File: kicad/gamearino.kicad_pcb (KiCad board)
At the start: 2 copper layers, 13 parts, among them Q1 FDN338P, Q2 FDN335N, Q3 PMBT3904, Q4 PMBT3906, SW1 Left, SW2 Up, SW3 Down, SW4 Right, SW5 Select, SW6 Start, SW7 B, SW8 A, U1 ESP-12F

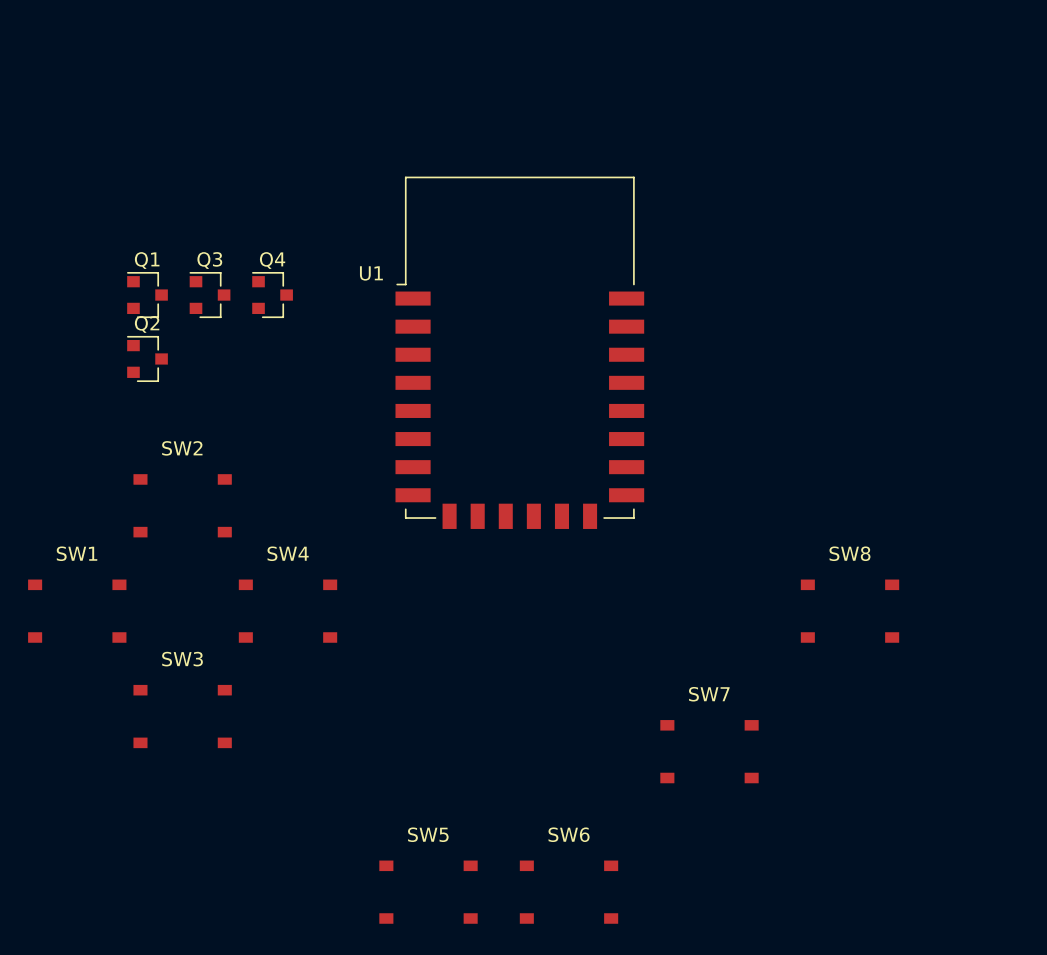
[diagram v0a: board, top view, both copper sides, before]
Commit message: PCB-Platzierung, 3D-Knöpfe, Schaltung wird noch getestet
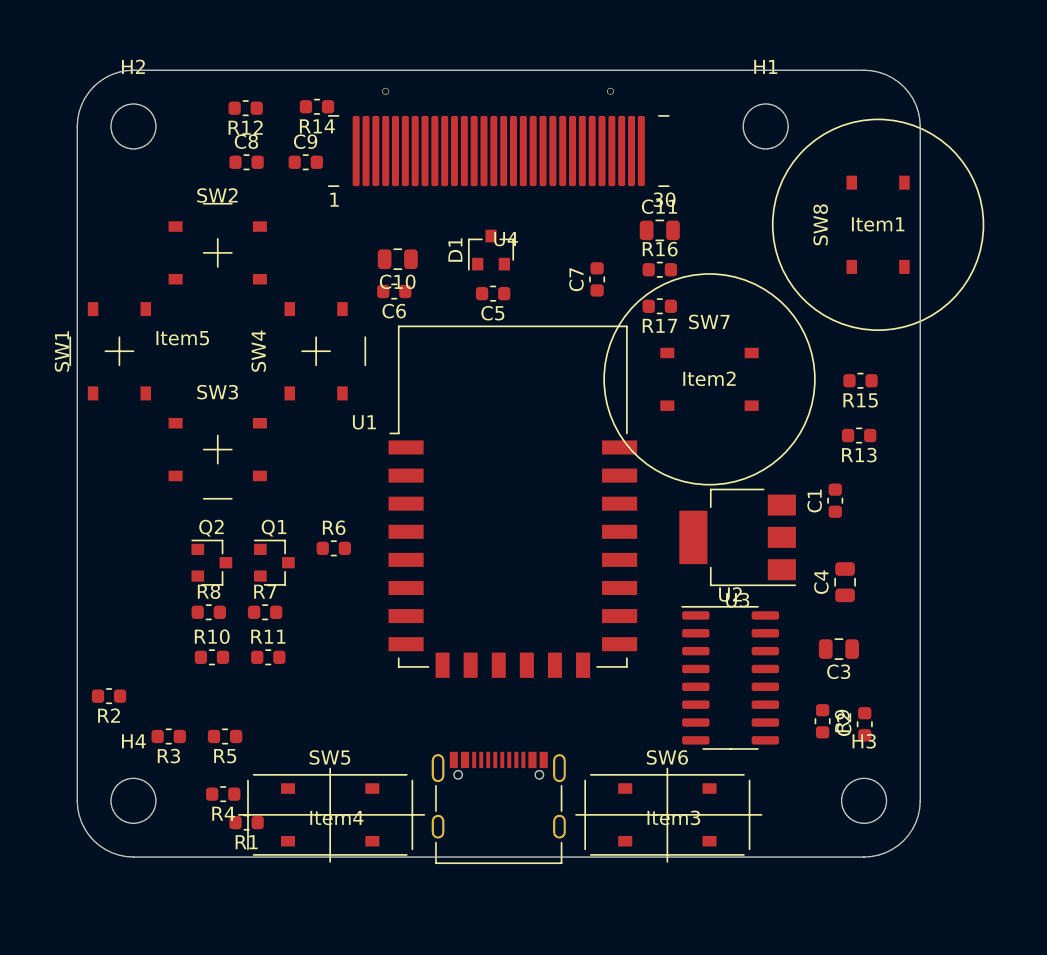
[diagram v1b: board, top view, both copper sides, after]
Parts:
- removed Q3: PMBT3904, Package_TO_SOT_SMD:SOT-23
- removed Q4: PMBT3906, Package_TO_SOT_SMD:SOT-23
- added C1: 100n, Capacitor_SMD:C_0603_1608Metric, F.Cu at (153.9, 74.6)
- added C10: 4u7, Capacitor_SMD:C_0805_2012Metric, F.Cu at (122.8, 57.5)
- added C11: 2u2, Capacitor_SMD:C_0805_2012Metric, F.Cu at (141.5, 55.4)
- added C2: 100n, Capacitor_SMD:C_0603_1608Metric, F.Cu at (156.1, 90.5)
- added C3: 10u/16V/X5R, Capacitor_SMD:C_0805_2012Metric, F.Cu at (154.2, 85.2)
- added C4: 10u/16V/X5R, Capacitor_SMD:C_0805_2012Metric, F.Cu at (154.7, 80.4)
- added C5: 1u, Capacitor_SMD:C_0603_1608Metric, F.Cu at (129.6, 59.9)
- added C6: 1u, Capacitor_SMD:C_0603_1608Metric, F.Cu at (122.6, 59.8)
- added C7: 1u, Capacitor_SMD:C_0603_1608Metric, F.Cu at (137.0, 58.9)
- added C8: 1u, Capacitor_SMD:C_0603_1608Metric, F.Cu at (112.0, 50.5)
- added C9: 1u, Capacitor_SMD:C_0603_1608Metric, F.Cu at (116.3, 50.5)
- added D1: 1N4148, Package_TO_SOT_SMD:SOT-23, F.Cu at (129.4, 56.8)
- added H1: MountingHole, MountingHole:MountingHole_3.2mm_M3, F.Cu at (149.0, 48.0)
- added H2: MountingHole, MountingHole:MountingHole_3.2mm_M3, F.Cu at (104.0, 48.0)
- added H3: MountingHole, MountingHole:MountingHole_3.2mm_M3, F.Cu at (156.0, 96.0)
- added H4: MountingHole, MountingHole:MountingHole_3.2mm_M3, F.Cu at (104.0, 96.0)
- added Item1: 3D Druck: Knopf A, gamearino:ABKnopf, F.Cu at (157.0, 55.0)
- added Item2: 3D Druck: Knopf B, gamearino:ABKnopf, F.Cu at (145.0, 66.0)
- added Item3: 3D Druck: Knopf Start, gamearino:StartSelect, F.Cu at (142.0, 97.0)
- added Item4: 3D Druck: Knopf Select, gamearino:StartSelect, F.Cu at (118.0, 97.0)
- added Item5: 3D Druck: Steuerkreuz, gamearino:Steuerkreuz_zeik, F.Cu at (110.0, 64.0)
- added J1: USB-C/16p, htl_connectors:USB_C_Receptacle_LCSC_C167321, F.Cu at (130.0, 95.6)
- added R1: 10k, Resistor_SMD:R_0603_1608Metric, F.Cu at (112.0, 97.5)
- added R10: 10k, Resistor_SMD:R_0603_1608Metric, F.Cu at (109.6, 85.8)
- added R11: R, Resistor_SMD:R_0603_1608Metric, F.Cu at (113.6, 85.8)
- added R12: 4k7, Resistor_SMD:R_0603_1608Metric, F.Cu at (112.0, 46.7)
- added R13: 10k, Resistor_SMD:R_0603_1608Metric, F.Cu at (155.7, 70.0)
- added R14: 4k7, Resistor_SMD:R_0603_1608Metric, F.Cu at (117.1, 46.6)
- added R15: 4k7, Resistor_SMD:R_0603_1608Metric, F.Cu at (155.8, 66.1)
- added R16: 4k7, Resistor_SMD:R_0603_1608Metric, F.Cu at (141.5, 58.2)
- added R17: 910k, Resistor_SMD:R_0603_1608Metric, F.Cu at (141.5, 60.8)
- added R2: 10k, Resistor_SMD:R_0603_1608Metric, F.Cu at (102.3, 88.5)
- added R3: 10k, Resistor_SMD:R_0603_1608Metric, F.Cu at (106.5, 91.4)
- added R4: R, Resistor_SMD:R_0603_1608Metric, F.Cu at (110.4, 95.5)
- added R5: R, Resistor_SMD:R_0603_1608Metric, F.Cu at (110.5, 91.4)
- added R6: 10k, Resistor_SMD:R_0603_1608Metric, F.Cu at (118.3, 78.0)
- added R7: R, Resistor_SMD:R_0603_1608Metric, F.Cu at (113.4, 82.6)
- added R8: 4k7, Resistor_SMD:R_0603_1608Metric, F.Cu at (109.4, 82.6)
- added R9: 100R, Resistor_SMD:R_0603_1608Metric, F.Cu at (153.1, 90.3)
- added U2: CH340C, Package_SO:SOIC-16_3.9x9.9mm_P1.27mm, F.Cu at (146.5, 87.2)
- added U3: AMS1117-3.3, Package_TO_SOT_SMD:SOT-223-3_TabPin2, F.Cu at (147.0, 77.2)
- added U4: QG-2864KSWEG01, gamearino:OLED_128x64_FlatRibbon_30, F.Cu at (130.0, 50.2)
- Q1: value FDN338P -> Q_NPN_BCE
- Q2: value FDN335N -> Q_NPN_BCE
- SW5: value Select -> Start
- SW6: value Start -> Select
- SW7: value B -> A
- SW8: value A -> B
- moved SW8 27.6 mm to (157.0, 55.0), turned to 90 degrees
- moved SW7 26.5 mm to (145.0, 66.0)
- moved Q1 21.1 mm to (114.0, 79.1)
- moved SW3 19.2 mm to (110.0, 71.0)
- moved SW1 18.7 mm to (103.0, 64.0), turned to 90 degrees
- moved SW4 18.6 mm to (117.0, 64.0), turned to 90 degrees
- moved SW2 18.2 mm to (110.0, 57.0)
- moved Q2 15.2 mm to (109.6, 79.1)
- moved U1 10.6 mm to (131.0, 74.3)
- moved SW5 8.90 mm to (118.0, 97.0)
- moved SW6 8.90 mm to (142.0, 97.0)
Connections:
- Q1 pad 1: (no net) -> Net-(Q1-Pad1)
- Q1 pad 2: (no net) -> /Auto-Reset/Reset
- Q1 pad 3: (no net) -> /Auto-Reset/RTS
- Q2 pad 1: (no net) -> Net-(Q2-Pad1)
- Q2 pad 2: (no net) -> /Auto-Reset/DTR
- Q2 pad 3: (no net) -> /Auto-Reset/GPIO0
- SW1 pad 1: Net-(SW1-Pad1) -> /Buttons/C0
- SW1 pad 2: Net-(SW1-Pad2) -> /Buttons/R1
- SW2 pad 1: Net-(SW2-Pad1) -> /Buttons/C0
- SW2 pad 2: Net-(SW2-Pad2) -> /Buttons/R0
- SW3 pad 1: Net-(SW3-Pad1) -> /Buttons/C0
- SW3 pad 2: Net-(SW3-Pad2) -> /Buttons/R2
- SW4 pad 1: Net-(SW4-Pad1) -> /Buttons/C1
- SW4 pad 2: Net-(SW4-Pad2) -> /Buttons/R2
- SW5 pad 1: Net-(SW5-Pad1) -> /Buttons/C1
- SW5 pad 2: Net-(SW5-Pad2) -> /Buttons/R0
- SW6 pad 1: Net-(SW6-Pad1) -> /Buttons/C1
- SW6 pad 2: Net-(SW6-Pad2) -> /Buttons/R1
- SW7 pad 1: Net-(SW7-Pad1) -> /Buttons/C2
- SW7 pad 2: Net-(SW7-Pad2) -> /Buttons/R1
- SW8 pad 1: Net-(SW8-Pad1) -> /Buttons/C2
- SW8 pad 2: Net-(SW8-Pad2) -> /Buttons/R0
- U1 pad 1: (no net) -> /Auto-Reset/Reset
- U1 pad 16: (no net) -> /Buttons/C0
- U1 pad 17: (no net) -> /OLED 128x64/SDA
- U1 pad 18: (no net) -> /Auto-Reset/GPIO0
- U1 pad 19: (no net) -> /Buttons/C1
- U1 pad 20: (no net) -> /Buttons/C2
- U1 pad 21: (no net) -> /USB/TxD
- U1 pad 22: (no net) -> /USB/RxD
- U1 pad 3: (no net) -> Net-(R1-Pad2)
- U1 pad 4: (no net) -> /Buttons/R0
- U1 pad 5: (no net) -> /OLED 128x64/SCL
- U1 pad 6: (no net) -> /Buttons/R1
- U1 pad 7: (no net) -> /Buttons/R2
- U1 pad 8: (no net) -> +3V3
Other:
- board outline added: 60 x 56 mm

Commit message: Gehäuse updates, Buttons richtig zugewiesen, Tetris
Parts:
- Q1, Q2: value Q_NPN_BCE -> PMBT3904,215
- R10: value 10k -> 100R
- R11: value R -> 100R
- R4, R5, R7: value R -> 10k
- SW5: value Start -> Select
- SW6: value Select -> Start
- SW7: value A -> B
- SW8: value B -> A
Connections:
- C1 pad 2: GNDD -> GND
- C10 pad 2: GNDD -> GND
- C11 pad 2: GNDD -> GND
- C2 pad 1: GNDD -> GND
- C3 pad 2: GNDD -> GND
- C4 pad 2: GNDD -> GND
- C5 pad 2: GNDD -> GND
- C6 pad 2: GNDD -> GND
- C7 pad 2: GNDD -> GND
- J1 pad A1: GNDD -> GND
- J1 pad A12: GNDD -> GND
- J1 pad B1: GNDD -> GND
- J1 pad B12: GNDD -> GND
- J1 pad S1: GNDD -> GND
- Q2 pad 2: /Auto-Reset/DTR -> /Auto-Reset/GPIO0
- Q2 pad 3: /Auto-Reset/GPIO0 -> /Auto-Reset/DTR
- R16 pad 2: GNDD -> GND
- R17 pad 1: GNDD -> GND
- R2 pad 2: GNDD -> GND
- R9 pad 2: GNDD -> GND
- U1 pad 15: (no net) -> GND
- U2 pad 1: GNDD -> GND
- U3 pad 1: GNDD -> GND
- U4 pad 1: GNDD -> GND
- U4 pad 10: GNDD -> GND
- U4 pad 12: GNDD -> GND
- U4 pad 13: GNDD -> GND
- U4 pad 16: GNDD -> GND
- U4 pad 17: GNDD -> GND
- U4 pad 21: GNDD -> GND
- U4 pad 22: GNDD -> GND
- U4 pad 23: GNDD -> GND
- U4 pad 24: GNDD -> GND
- U4 pad 25: GNDD -> GND
- U4 pad 29: GNDD -> GND
- U4 pad 30: GNDD -> GND
- U4 pad 8: GNDD -> GND

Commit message: v0.0.1 für CNC-Fertigung
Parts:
- H1, H2, H3, H4: footprint MountingHole:MountingHole_3.2mm_M3 -> htl_mechanical:MountingHole_3.2mm_M3
- moved R8 49.2 mm to (158.2, 76.7), turned to 90 degrees
- moved Q2 48.0 mm to (157.2, 73.2), turned to 90 degrees
- moved R7 43.3 mm to (156.2, 76.8), turned to 270 degrees
- moved R2 42.9 mm to (144.7, 82.0), turned to 0 degrees
- moved C4 42.2 mm to (113.0, 87.5), turned to 270 degrees
- moved C3 41.2 mm to (113.0, 83.5), turned to 270 degrees
- moved U3 40.3 mm to (107.6, 85.5)
- moved Q1 39.4 mm to (153.0, 73.2), turned to 90 degrees
- moved R15 35.6 mm to (121.0, 58.5), turned to 90 degrees
- moved R6 33.8 mm to (152.0, 76.8), turned to 270 degrees
- moved R10 33.2 mm to (142.8, 84.5), turned to 180 degrees
- moved R11 29.2 mm to (142.8, 86.0)
- moved R13 28.1 mm to (130.0, 58.5), turned to 270 degrees
- moved R12 26.1 mm to (135.2, 58.5), turned to 270 degrees
- moved R14 23.2 mm to (137.0, 58.5), turned to 270 degrees
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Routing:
- net /Buttons/R0: track 0.00 -> 154.5 mm
- net /Buttons/R1: track 0.00 -> 147.1 mm, vias 0 -> 6
- net +3V3: track 0.00 -> 142.7 mm, vias 0 -> 4
- net GND: track 0.00 -> 99.1 mm, vias 0 -> 24
- net /Buttons/C0: track 0.00 -> 84.4 mm, vias 0 -> 2
- net /Buttons/C1: track 0.00 -> 83.5 mm, vias 0 -> 4
- net /Auto-Reset/Reset: track 0.00 -> 58.5 mm, vias 0 -> 2
- net /OLED 128x64/SCL: track 0.00 -> 57.8 mm, vias 0 -> 3
- net Net-(C3-Pad1): track 0.00 -> 55.1 mm, vias 0 -> 2
- net /OLED 128x64/SDA: track 0.00 -> 41.6 mm, vias 0 -> 2
- net /Buttons/C2: track 0.00 -> 34.3 mm
- net /Buttons/R2: track 0.00 -> 34.2 mm, vias 0 -> 2
- net /Auto-Reset/DTR: track 0.00 -> 27.8 mm, vias 0 -> 2
- net Net-(D1-Pad1): track 0.00 -> 24.8 mm, vias 0 -> 2
- net /Auto-Reset/GPIO0: track 0.00 -> 24.4 mm
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- added copper zone on B.Cu, net GND
- added copper zone on F.Cu, net GND
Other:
- net class Default: clearance 0.2 -> 0.25; via_dia 0.8 -> 0.9
- rule trace_clearance: 0.2 -> 0.25
- board text added: "Gamearino v0.0.1"

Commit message: Fertiges Layout v0.0.2, 3 Stk bestellt
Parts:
- added C12: 1u, Capacitor_SMD:C_0603_1608Metric, F.Cu at (144.8, 58.5)
- added D2: LED_Dual_green-red, htl_smd:LED_LiteOn_LTST-C195KGJRKT, F.Cu at (110.0, 49.0)
- added FID1: Fiducial, htl_mechanical:paste-fiducial, F.Cu at (110.0, 47.0)
- added FID2: Fiducial, htl_mechanical:paste-fiducial, F.Cu at (155.0, 92.0)
- added R10: 5k1, Resistor_SMD:R_0603_1608Metric, F.Cu at (137.2, 91.7)
- added R20: 4k7, Resistor_SMD:R_0603_1608Metric, F.Cu at (102.0, 53.0)
- added R9: 5k1, Resistor_SMD:R_0603_1608Metric, F.Cu at (123.5, 92.0)
- C10: value 4u7 -> 10u/16V/X5R
- C11: value 2u2 -> 1u; footprint Capacitor_SMD:C_0805_2012Metric -> Capacitor_SMD:C_0603_1608Metric
- D1: value 1N4148 -> BAV99
- Item1, Item2: footprint gamearino:ABKnopf -> gamearino:ABKnopf_v2
- Item3, Item4: footprint gamearino:StartSelect -> gamearino:StartSelect_v2
- Item5: footprint gamearino:Steuerkreuz_zeik -> gamearino:Steuerkreuz_zeik_v2
- moved C10 0.25 mm to (141.0, 58.5)
- turned D1 to 270 degrees
- renumbered R9 to R11, R10 to R12, R11 to R13, R12 to R14, R13 to R15, R14 to R16, R15 to R17, R16 to R18, R17 to R19, J1 to X1
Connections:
- net Net-(R1-Pad2) renamed /EN
- D1 pad 1: Net-(D1-Pad1) -> Net-(C5-Pad1)
- D1 pad 2: Net-(C5-Pad1) -> (no net)
- D1 pad 3: (no net) -> Net-(D1-Pad3)
- R14 pad 2: Net-(D1-Pad1) -> Net-(D1-Pad3)
- R16 pad 2: Net-(D1-Pad1) -> Net-(D1-Pad3)
- U2 pad 10: (no net) -> GND
- U2 pad 11: (no net) -> GND
- U2 pad 12: (no net) -> GND
- U2 pad 9: (no net) -> GND
- U4 pad 11: Net-(D1-Pad1) -> Net-(D1-Pad3)
- X1 pad A5: (no net) -> Net-(R9-Pad2)
- X1 pad B5: (no net) -> Net-(R10-Pad1)
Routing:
- net Net-(D1-Pad3): track 0.00 -> 25.4 mm, vias 0 -> 2
- net Net-(D1-Pad1): track 24.8 -> 0.00 mm, vias 2 -> 0
- net Net-(C3-Pad1): track 55.1 -> 71.6 mm, vias 2 -> 4
- net /Buttons/C0: track 84.4 -> 97.1 mm, vias 2 -> 6
- net /Buttons/R2: track 34.2 -> 46.1 mm, vias 2 -> 6
- net /Buttons/R1: track 147.1 -> 158.9 mm, vias 6 -> 8
- net GND: track 99.1 -> 109.2 mm, vias 24 -> 50
- net Net-(D2-Pad2): track 0.00 -> 9.16 mm
- net /Buttons/R0: track 154.5 -> 163.5 mm
- net Net-(R10-Pad1): track 0.00 -> 8.25 mm
- net Net-(R9-Pad2): track 0.00 -> 8.19 mm
- net /Buttons/C1: track 83.5 -> 89.5 mm, vias 4 -> 6
- net /Buttons/C2: track 34.3 -> 40.3 mm
- net /USB/D-: track 23.9 -> 21.2 mm
- net Net-(C6-Pad1): track 17.7 -> 20.1 mm
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- added copper zone on B.Cu, net +3V3
- added copper zone on F.Cu, net +3V3
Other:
- net class Default: clearance 0.25 -> 0.15; trace_width 0.25 -> 0.15
- rule trace_clearance: 0.25 -> 0.15
- rule trace_min: 0.2 -> 0.15
- board text added: "A"
- board text added: "AMS1117-3.3"
- board text added: "B"
- board text added: "CH340C"
- board text added: "DOWN"
- board text added: "ESP-12F (ESP8266) Arduino IDE settings compatible with NodeMCU V1.0"
- board text added: "Gamearino V0.0.2"
- board text added: "HTL STEYR 2021"
- board text added: "LEFT"
- board text added: "RIGHT"
- board text added: "SELECT"
- board text added: "START"
- board text added: "UP"
- board text added: "V0.0.2"
- board text added: "github.com/KarlZeilhofer/gamearino"
- board text removed: "Gamearino v0.0.1"

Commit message: Layoutbugfixes, v20.0.3 fertig, CAM-Daten
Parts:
- removed R17, R18: 4k7, Resistor_SMD:R_0603_1608Metric
- added C13: DNP, Capacitor_SMD:C_0603_1608Metric, F.Cu at (117.5, 71.5)
- added SW9: Reset, htl_smd:SW_Push_5.1mm_H1.5mm, F.Cu at (115.0, 47.0)
- turned R15 to 90 degrees
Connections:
- C6 pad 1: Net-(C6-Pad1) -> +3V3
- C7 pad 1: Net-(C6-Pad1) -> +3V3
- D1 pad 3: Net-(D1-Pad3) -> +3V3
- Q1 pad 2: /Auto-Reset/Reset -> /Auto-Reset/RTS
- Q1 pad 3: /Auto-Reset/RTS -> /~RESET
- Q2 pad 2: /Auto-Reset/GPIO0 -> /Auto-Reset/DTR
- Q2 pad 3: /Auto-Reset/DTR -> /Auto-Reset/GPIO0
- R14 pad 1: /OLED 128x64/SDA -> /OLED 128x64/SCL
- R14 pad 2: Net-(D1-Pad3) -> +3V3
- R15 pad 1: Net-(C5-Pad1) -> +3V3
- R15 pad 2: +3V3 -> Net-(C5-Pad1)
- R16 pad 1: /OLED 128x64/SCL -> /OLED 128x64/SDA
- R16 pad 2: Net-(D1-Pad3) -> +3V3
- U1 pad 1: /Auto-Reset/Reset -> /~RESET
- U1 pad 17: /OLED 128x64/SDA -> /OLED 128x64/SCL
- U1 pad 5: /OLED 128x64/SCL -> /OLED 128x64/SDA
- U4 pad 11: Net-(D1-Pad3) -> +3V3
- U4 pad 15: Net-(R18-Pad1) -> GND
- U4 pad 18: /OLED 128x64/SDA -> /OLED 128x64/SCL
- U4 pad 19: /OLED 128x64/SCL -> /OLED 128x64/SDA
- U4 pad 20: /OLED 128x64/SCL -> /OLED 128x64/SDA
- U4 pad 6: Net-(C6-Pad1) -> +3V3
- U4 pad 9: Net-(C6-Pad1) -> +3V3
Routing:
- net /~RESET: track 0.00 -> 82.1 mm, vias 0 -> 3
- net /Auto-Reset/Reset: track 59.9 -> 0.00 mm, vias 2 -> 0
- net +3V3: track 144.3 -> 189.7 mm
- net Net-(D1-Pad3): track 25.4 -> 0.00 mm, vias 2 -> 0
- net Net-(C6-Pad1): track 20.1 -> 0.00 mm
- net /OLED 128x64/SCL: track 58.4 -> 40.2 mm, vias 3 -> 2
- net /OLED 128x64/SDA: track 40.5 -> 58.0 mm, vias 2 -> 3
- net Net-(R18-Pad1): track 9.56 -> 0.00 mm
- net Net-(C3-Pad1): track 71.6 -> 65.6 mm
- net /Auto-Reset/DTR: track 27.8 -> 31.2 mm
- net /Auto-Reset/RTS: track 19.3 -> 16.9 mm
- net /Auto-Reset/GPIO0: track 24.6 -> 27.0 mm
- net GND: track 109.2 -> 107.6 mm, vias 50 -> 53
- net /Buttons/R0: track 163.5 -> 163.2 mm, vias 0 -> 2
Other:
- board text added: "Gamearino V20.0.3"
- board text added: "V20.0.3"
- board text removed: "Gamearino V0.0.2"
- board text removed: "V0.0.2"
